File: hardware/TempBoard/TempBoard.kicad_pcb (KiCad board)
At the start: 2 copper layers, 30 x 30 mm, 19 parts, among them J2 Conn_01x04, J3 Conn_01x05, U1 BME280

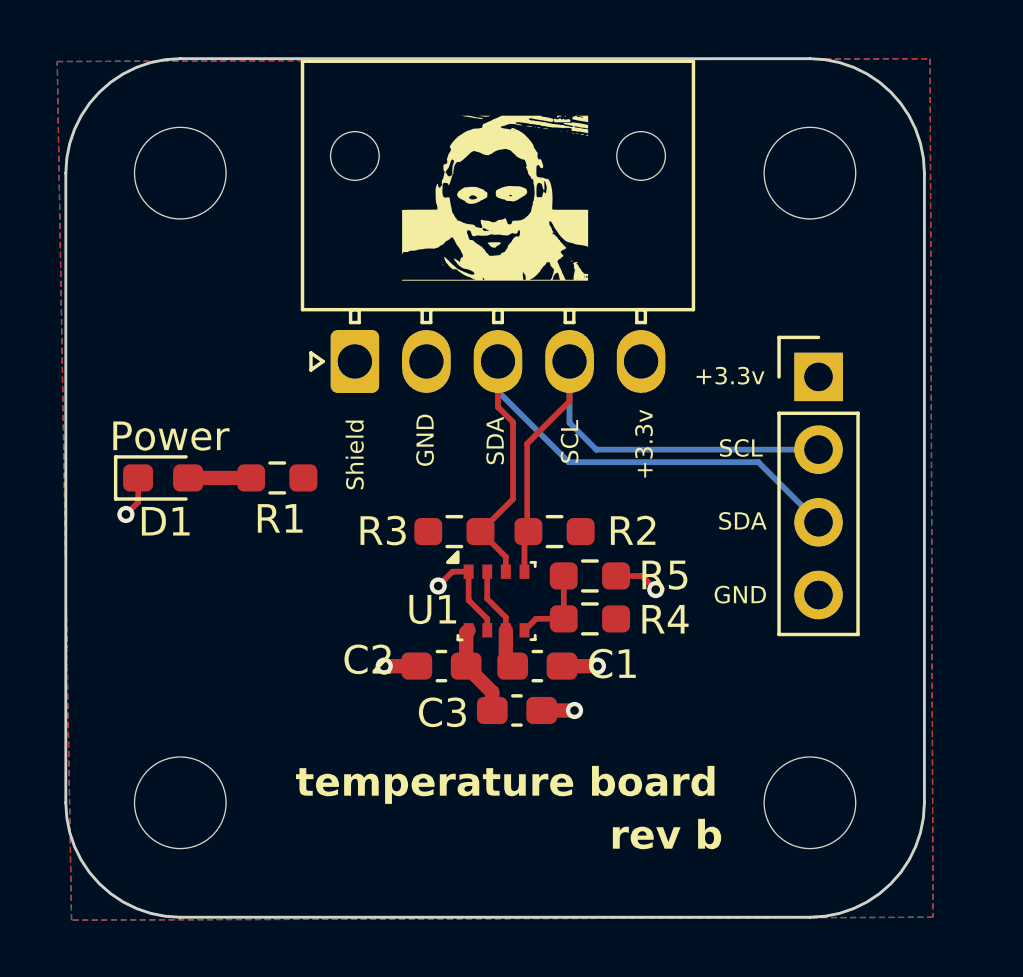
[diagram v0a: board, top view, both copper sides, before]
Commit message: resized temperature board
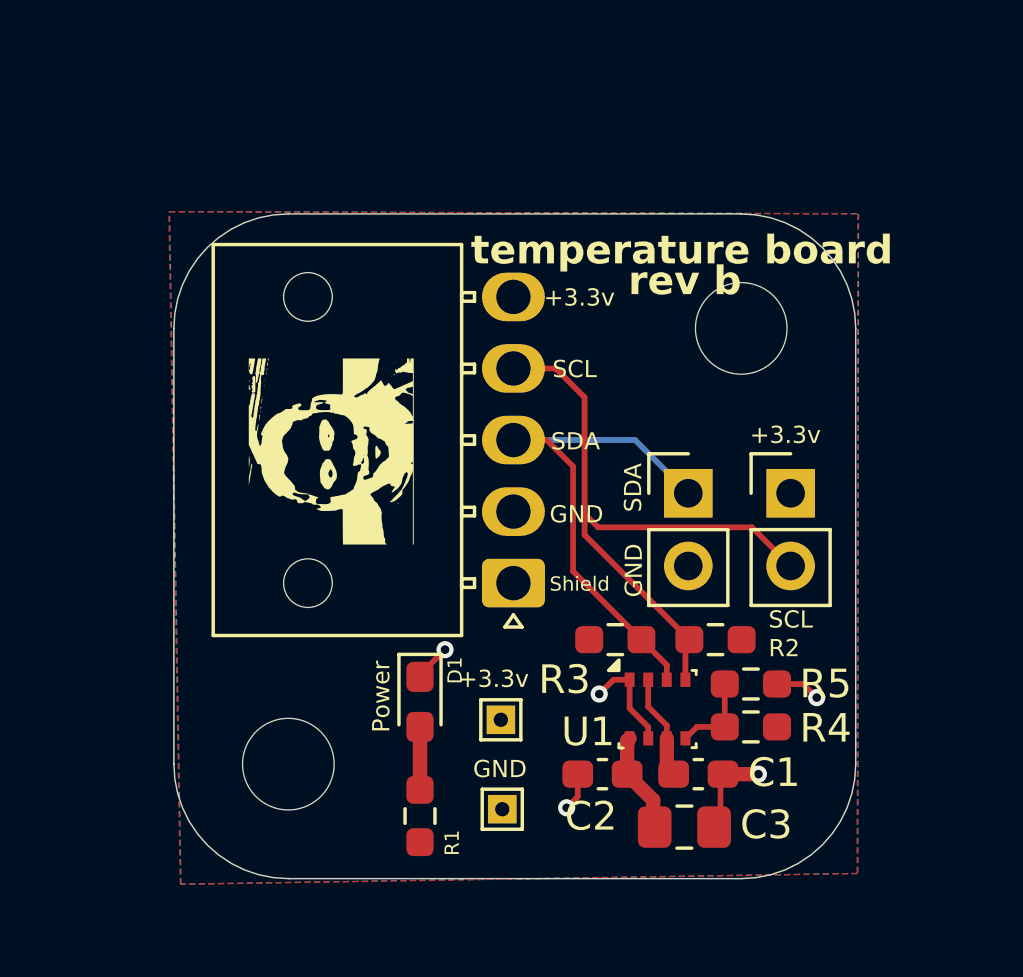
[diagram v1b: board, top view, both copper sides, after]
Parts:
- removed H3, H4: MountingHole, MountingHole:MountingHole_3.2mm_M3
- removed J2: Conn_01x04, Connector_PinHeader_2.54mm:PinHeader_1x04_P2.54mm_Vertical
- added 3.3vTP1: TestPoint, TestPoint:TestPoint_THTPad_1.0x1.0mm_Drill0.5mm, F.Cu at (130.9, 77.0)
- added GND_TP1: TestPoint, TestPoint:TestPoint_THTPad_1.0x1.0mm_Drill0.5mm, F.Cu at (130.9, 80.1)
- added J1: Conn_01x02, Connector_PinHeader_2.54mm:PinHeader_1x02_P2.54mm_Vertical, F.Cu at (141.0, 69.1)
- added J4: Conn_01x02, Connector_PinHeader_2.54mm:PinHeader_1x02_P2.54mm_Vertical, F.Cu at (137.4, 69.1)
- C3: footprint Capacitor_SMD:C_0603_1608Metric_Pad1.08x0.95mm_HandSolder -> Capacitor_SMD:C_0805_2012Metric_Pad1.18x1.45mm_HandSolder
- moved H1 20.3 mm to (139.3, 63.3)
- moved H2 18.3 mm to (123.5, 78.5)
- moved G*** 15.5 mm to (127.8, 66.0)
- moved R1 12.8 mm to (128.1, 80.4), turned to 90 degrees
- moved D1 11.9 mm to (128.1, 76.4), turned to -90 degrees
- moved G*** 10.5 mm to (125.0, 67.6), turned to 90 degrees
- moved J3 9.52 mm to (131.3, 72.2), turned to 180 degrees
- moved C3 7.13 mm to (137.3, 80.8)
- moved C1 6.77 mm to (137.8, 78.9)
- moved C2 6.77 mm to (134.4, 78.9)
- moved R2 6.77 mm to (138.4, 74.2)
- moved R3 6.77 mm to (134.9, 74.2)
- moved R4 6.77 mm to (139.6, 77.2)
- moved R5 6.77 mm to (139.6, 75.8)
- moved U1 6.77 mm to (136.4, 76.6)
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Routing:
- net /SDA: track 23.9 -> 18.2 mm
- net /SCL: track 19.7 -> 22.4 mm
- net GND: track 10.2 -> 11.0 mm, vias 6 -> 5
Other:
- board size 30 x 30 mm -> 23.8 x 23.2 mm
- board text added: "karthik kurapati febuary 2026"
- board text added: "validated"
- board text removed: "Karthik Kurapati Febuary 2026"

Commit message: poo oo ee
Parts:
- R1: value 1k -> 470
- R2, R3: value 4.7k -> 10k
- moved C3 0.13 mm to (137.3, 80.6)
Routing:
- net /SCL: track 22.4 -> 22.3 mm, vias 0 -> 1
